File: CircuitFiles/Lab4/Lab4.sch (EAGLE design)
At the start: 16 parts, among them Q1 TIP120, U1 OPA2350N

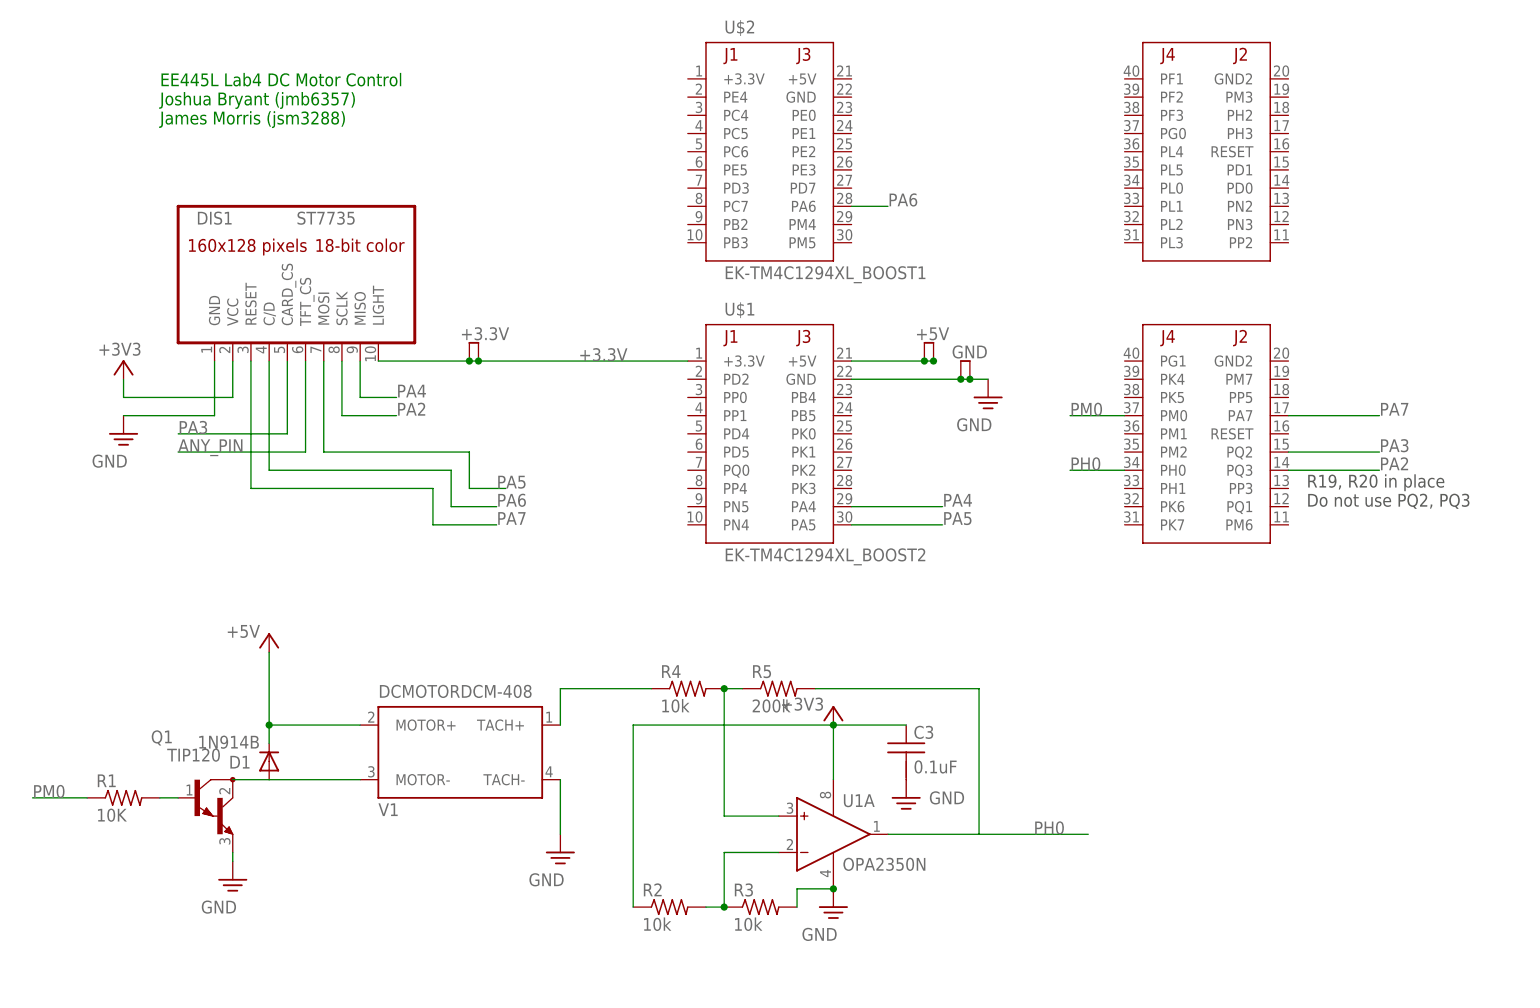
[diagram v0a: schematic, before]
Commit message: Lab 4 Report added and Lab 4&5 files updated
Updated the schematic for Lab 4 to reflect the final design change to
the circuitry between the tachometer output and the OPA2350 input.

Added files for Lab 4 report. Need to add data measurements and data
analysis and it'll be ready to turn in.

Doing initial add of Lab 5 files including the Lab 5 prep and Lab5
circuit.
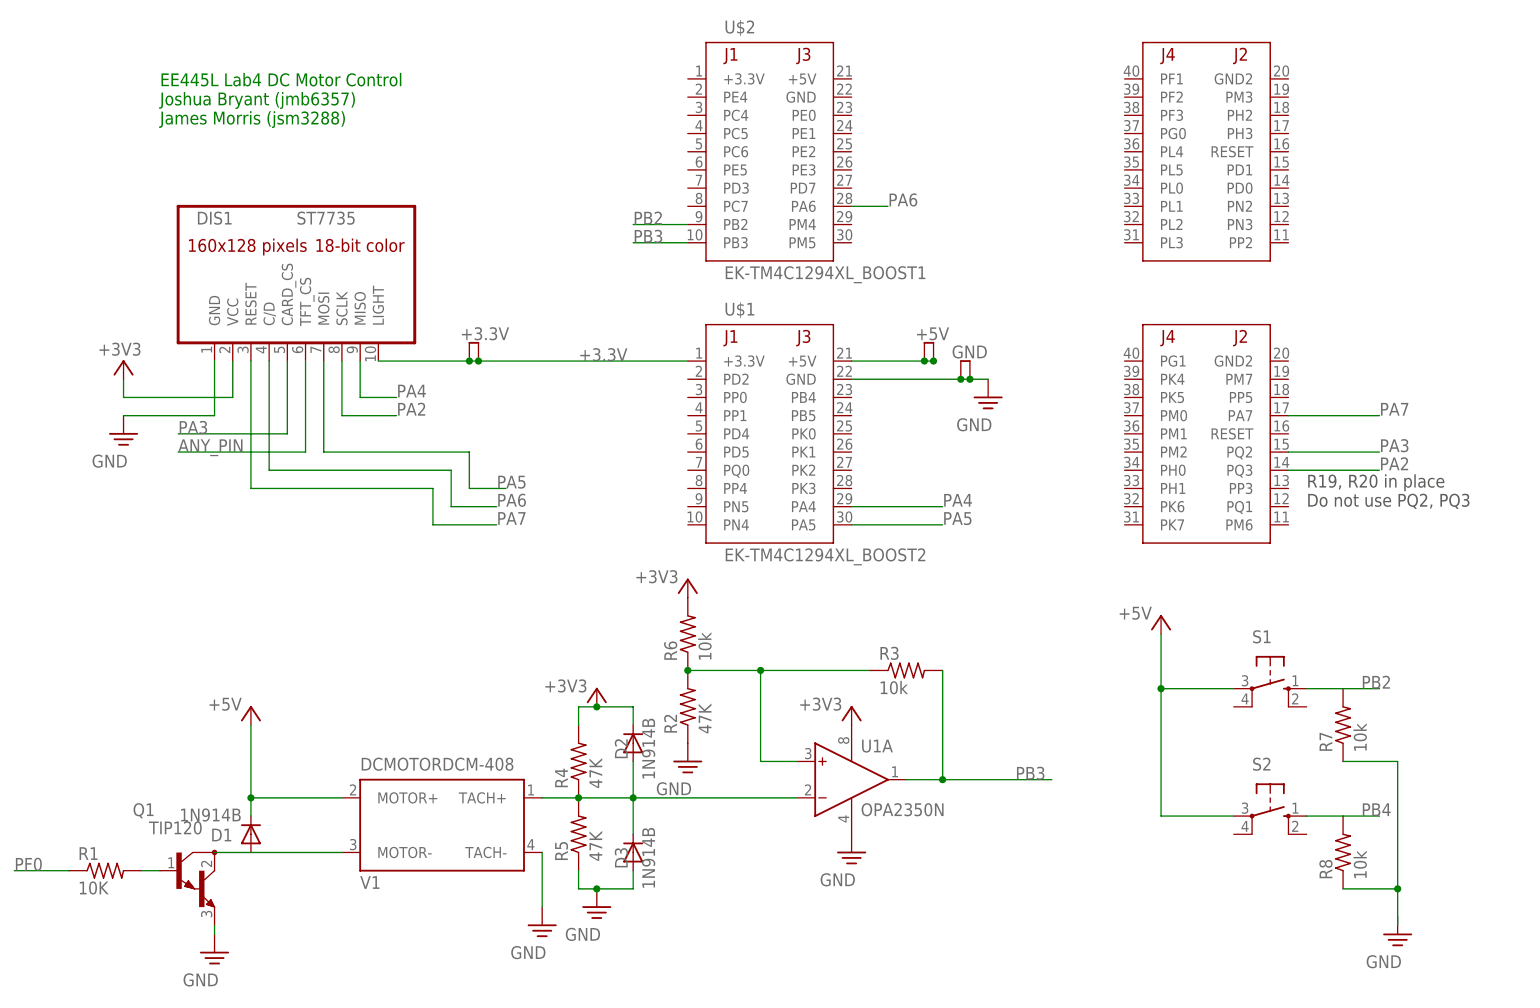
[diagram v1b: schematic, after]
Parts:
- removed C3: 0.1uF, EE445L:CAPACITOR025-024X044
- added D2, D3: 1N914B, EE445L:1N914B
- added R6, R7, R8: 10k, rcl:R-US_0204/2V
- added S1, S2: (no value), EE445L:B3F-1052
- R2, R4: value 10k -> 47K
- R5: value 200k -> 47K
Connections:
- removed net N$5: R4.2, R5.1, U1A.IN+
- removed net PH0: R5.2, U$1.PH0, U1A.OUT
- removed net PM0: R1.1, U$1.PM0
- new net N$8: R7.1, R8.1
- new net PB2: R7.2, S1.S
- new net PB3: R3.2, U1A.OUT
- new net PB4: R8.2, S2.S
- new net PF0: R1.1
- net +3V3: now also D2.C, R4.2, R6.2, S1.P, S2.P; no longer C3.1, R2.1
- net GND: now also D3.A, R2.1, R5.1; no longer C3.2, R3.2
- net N$1: now also D2.A, D3.C, R4.1, R5.2, V1.TACH+; no longer R2.2, R3.1
- net N$7: now also R2.2, R3.1, R6.1, U1A.IN+; no longer R4.1, V1.TACH+
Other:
- moved on the sheet: D1, Q1, R1, R2, R3, R4, R5, U1A, V1
